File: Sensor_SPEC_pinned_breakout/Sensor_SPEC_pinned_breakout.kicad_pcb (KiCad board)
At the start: 2 copper layers, 42 x 26 mm, 5 parts, among them P1 CONN_01X04, U1 SPEC, U2 SMM-102-02-S-S, U3 SMM-102-02-S-S, U4 SMM-102-02-S-S

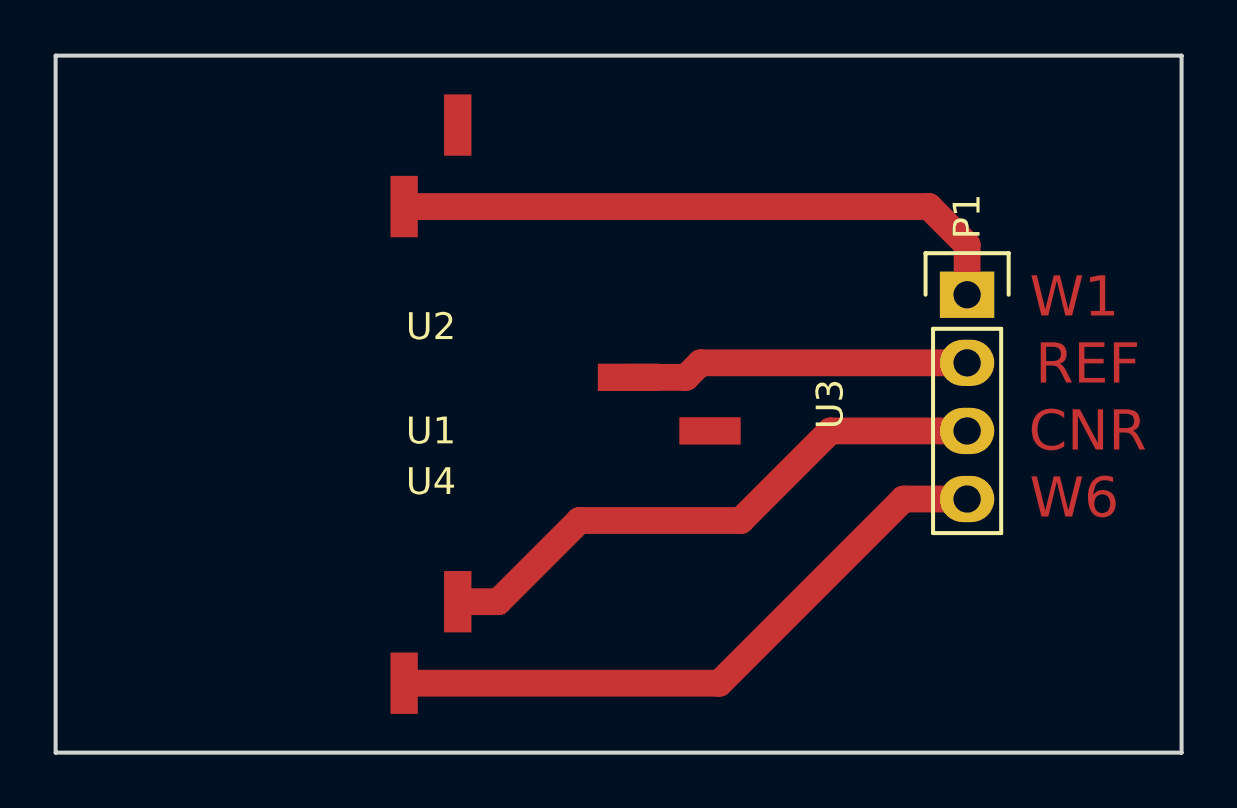
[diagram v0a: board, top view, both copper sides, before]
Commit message: changed SPEC pinned breakout
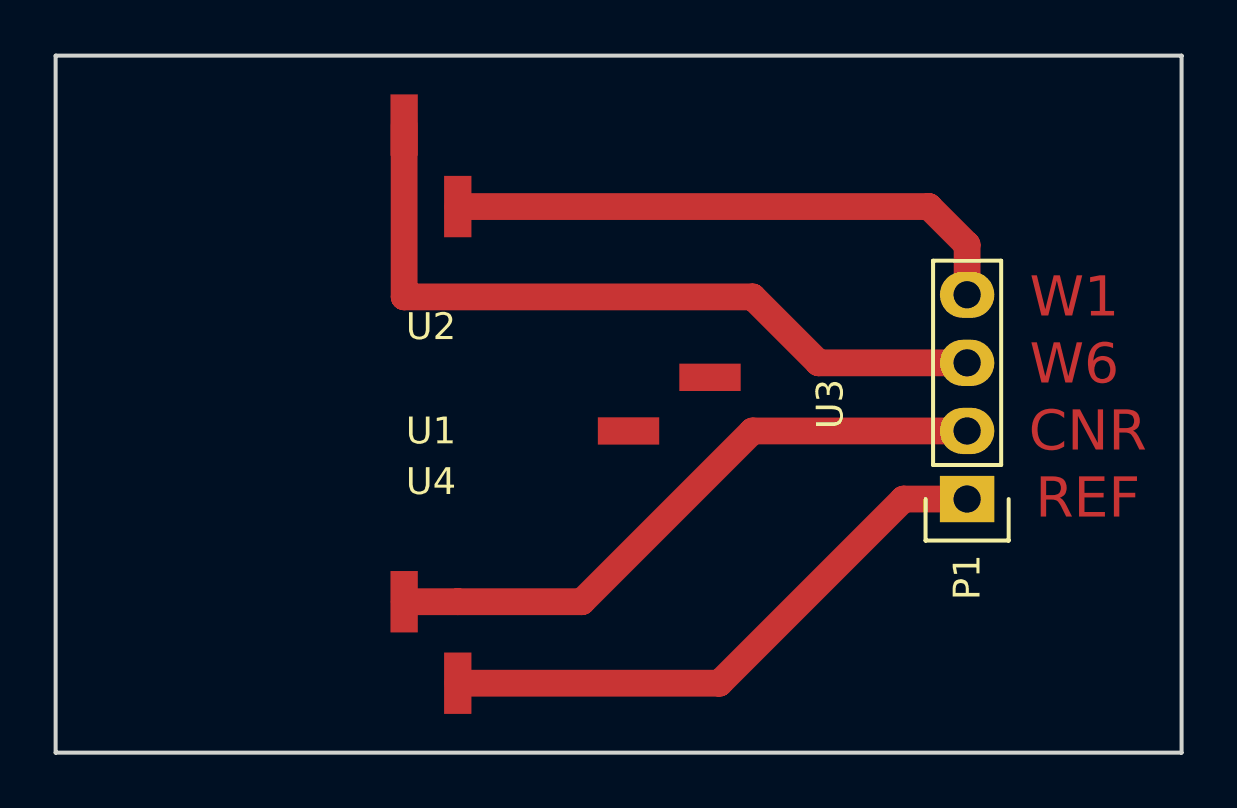
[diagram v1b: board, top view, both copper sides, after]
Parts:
- moved P1 7.62 mm to (168.0, 110.5), turned to 90 degrees
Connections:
- P1 pad 1: WORKING_1 -> REFERENCE
- P1 pad 2: REFERENCE -> COUNTER
- P1 pad 3: COUNTER -> WORKING_6
- P1 pad 4: WORKING_6 -> WORKING_1
- U2 pad 2: Net-(U2-Pad2) -> WORKING_6
- U3 pad 2: REFERENCE -> Net-(U3-Pad2)
- U4 pad 2: WORKING_6 -> REFERENCE
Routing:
- net REFERENCE: track 12.9 -> 21.8 mm
- net WORKING_6: track 23.8 -> 28.4 mm
- net WORKING_1: track 23.5 -> 21.5 mm
- net COUNTER: track 21.6 -> 23.6 mm
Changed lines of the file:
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@@
     (links 4)
     (no_connects 0)
-    (area 0 0 0 0)
+    (area 133.924999 93.924999 176.075001 120.075001)
     (thickness 1.6)
     (drawings 8)
@@
     (visible_elements FFFFFF7F)
     (pcbplotparams
-      (layerselection 0x00030_80000001)
+      (layerselection 0x01000_00000001)
       (usegerberextensions false)
       (excludeedgelayer true)
@@
       (outputformat 1)
       (mirror false)
-      (drillshape 1)
+      (drillshape 0)
       (scaleselection 1)
-      (outputdirectory ""))
+      (outputdirectory gerbers/))
   )
   (net 0 "")
@@
   (net 3 COUNTER)
   (net 4 WORKING_6)
-  (net 5 "Net-(U2-Pad2)")
-  (net 6 "Net-(U3-Pad1)")
+  (net 5 "Net-(U3-Pad1)")
+  (net 6 "Net-(U3-Pad2)")
   (net_class Default "This is the default net class."
     (clearance 0.2)
@@
     (uvia_drill 0.1)
     (add_net COUNTER)
-    (add_net "Net-(U2-Pad2)")
     (add_net "Net-(U3-Pad1)")
+    (add_net "Net-(U3-Pad2)")
     (add_net REFERENCE)
     (add_net WORKING_1)
@@
   )
   (module Socket_Strips:Socket_Strip_Straight_1x04 (layer F.Cu)
-    (at 168 102.92 270)
+    (at 168 110.54 90)
     (descr "Through hole socket strip")
     (tags "socket strip")
-    (fp_text reference P1 (at -2.92 0 270) (layer F.SilkS)
-      (effects (font (size 1 1) (thickness 0.15)))
-    )
-    (fp_text value CONN_01X04 (at 4.08 3 270) (layer F.Fab)
+    (fp_text reference P1 (at -2.92 0 90) (layer F.SilkS)
+      (effects (font (size 1 1) (thickness 0.15)))
+    )
+    (fp_text value CONN_01X04 (at 4.08 -3 90) (layer F.Fab)
       (effects (font (size 1 1) (thickness 0.15)))
     )
@@
     (fp_line (start 0 -1.55) (end -1.55 -1.55) (layer F.SilkS) (width 0.15))
     (fp_line (start -1.55 -1.55) (end -1.55 1.55) (layer F.SilkS) (width 0.15))
-    (pad 1 thru_hole rect (at 0 0 270) (size 1.7272 2.032) (drill 1.016) (layers *.Cu *.Mask F.SilkS)
+    (pad 1 thru_hole rect (at 0 0 90) (size 1.7272 2.032) (drill 1.016) (layers *.Cu *.Mask F.SilkS)
+      (net 2 REFERENCE))
+    (pad 2 thru_hole oval (at 2.54 0 90) (size 1.7272 2.032) (drill 1.016) (layers *.Cu *.Mask F.SilkS)
+      (net 3 COUNTER))
+    (pad 3 thru_hole oval (at 5.08 0 90) (size 1.7272 2.032) (drill 1.016) (layers *.Cu *.Mask F.SilkS)
+      (net 4 WORKING_6))
+    (pad 4 thru_hole oval (at 7.62 0 90) (size 1.7272 2.032) (drill 1.016) (layers *.Cu *.Mask F.SilkS)
       (net 1 WORKING_1))
-    (pad 2 thru_hole oval (at 2.54 0 270) (size 1.7272 2.032) (drill 1.016) (layers *.Cu *.Mask F.SilkS)
-      (net 2 REFERENCE))
-    (pad 3 thru_hole oval (at 5.08 0 270) (size 1.7272 2.032) (drill 1.016) (layers *.Cu *.Mask F.SilkS)
-      (net 3 COUNTER))
-    (pad 4 thru_hole oval (at 7.62 0 270) (size 1.7272 2.032) (drill 1.016) (layers *.Cu *.Mask F.SilkS)
-      (net 4 WORKING_6))
     (model Socket_Strips.3dshapes/Socket_Strip_Straight_1x04.wrl
       (at (xyz 0.15 0 0))
@@
       (effects (font (size 1 1) (thickness 0.15)))
     )
-    (pad 1 smd rect (at -1 1.52) (size 1.02 2.29) (layers F.Cu F.Paste F.Mask)
+    (pad 1 smd rect (at 1 1.52) (size 1.02 2.29) (layers F.Cu F.Paste F.Mask)
       (net 1 WORKING_1))
-    (pad 2 smd rect (at 1 -1.52) (size 1.02 2.29) (layers F.Cu F.Paste F.Mask)
-      (net 5 "Net-(U2-Pad2)"))
+    (pad 2 smd rect (at -1 -1.52) (size 1.02 2.29) (layers F.Cu F.Paste F.Mask)
+      (net 4 WORKING_6))
+  )
+  (module scintilla:SMM-102-02-S-S (layer F.Cu)
+    (at 148 115.89 180)
+    (fp_text reference U4 (at 0 6 180) (layer F.SilkS)
+      (effects (font (size 1 1) (thickness 0.15)))
+    )
+    (fp_text value SMM-102-02-S-S (at 0 -6 180) (layer F.Fab)
+      (effects (font (size 1 1) (thickness 0.15)))
+    )
+    (pad 1 smd rect (at 1 1.52 180) (size 1.02 2.29) (layers F.Cu F.Paste F.Mask)
+      (net 3 COUNTER))
+    (pad 2 smd rect (at -1 -1.52 180) (size 1.02 2.29) (layers F.Cu F.Paste F.Mask)
+      (net 2 REFERENCE))
   )
   (module scintilla:SMM-102-02-S-S (layer F.Cu)
@@
       (effects (font (size 1 1) (thickness 0.15)))
     )
-    (pad 1 smd rect (at -1 1.52 90) (size 1.02 2.29) (layers F.Cu F.Paste F.Mask)
-      (net 6 "Net-(U3-Pad1)"))
-    (pad 2 smd rect (at 1 -1.52 90) (size 1.02 2.29) (layers F.Cu F.Paste F.Mask)
-      (net 2 REFERENCE))
-  )
-  (module scintilla:SMM-102-02-S-S (layer F.Cu)
-    (at 148 115.89 180)
-    (fp_text reference U4 (at 0 6 180) (layer F.SilkS)
-      (effects (font (size 1 1) (thickness 0.15)))
-    )
-    (fp_text value SMM-102-02-S-S (at 0 -6 180) (layer F.Fab)
-      (effects (font (size 1 1) (thickness 0.15)))
-    )
-    (pad 1 smd rect (at -1 1.52 180) (size 1.02 2.29) (layers F.Cu F.Paste F.Mask)
-      (net 3 COUNTER))
-    (pad 2 smd rect (at 1 -1.52 180) (size 1.02 2.29) (layers F.Cu F.Paste F.Mask)
-      (net 4 WORKING_6))
+    (pad 1 smd rect (at 1 1.52 90) (size 1.02 2.29) (layers F.Cu F.Paste F.Mask)
+      (net 5 "Net-(U3-Pad1)"))
+    (pad 2 smd rect (at -1 -1.52 90) (size 1.02 2.29) (layers F.Cu F.Paste F.Mask)
+      (net 6 "Net-(U3-Pad2)"))
+  )
+  (gr_text REF (at 172.5 110.5) (layer F.Cu)
+    (effects (font (size 1.5 1.5) (thickness 0.3)))
   )
   (gr_line (start 134 120) (end 134 94) (layer Edge.Cuts) (width 0.15))
@@
   (gr_line (start 176 94) (end 176 120) (layer Edge.Cuts) (width 0.15))
   (gr_line (start 134 94) (end 176 94) (layer Edge.Cuts) (width 0.15))
-  (gr_text W6 (at 172 110.5) (layer F.Cu)
+  (gr_text W6 (at 172 105.5) (layer F.Cu)
     (effects (font (size 1.5 1.5) (thickness 0.3)))
   )
@@
     (effects (font (size 1.5 1.5) (thickness 0.3)))
   )
-  (gr_text REF (at 172.5 105.5) (layer F.Cu)
-    (effects (font (size 1.5 1.5) (thickness 0.3)))
-  )
   (gr_text W1 (at 172 103) (layer F.Cu)
     (effects (font (size 1.5 1.5) (thickness 0.3)))
   )
-  (segment (start 147 99.63) (end 166.5736 99.63) (width 1) (layer F.Cu) (net 1))
+  (segment (start 166.5736 99.63) (end 149 99.63) (width 1) (layer F.Cu) (net 1))
   (segment (start 166.5736 99.63) (end 168 101.0564) (width 1) (layer F.Cu) (net 1))
   (segment (start 168 101.0564) (end 168 102.92) (width 1) (layer F.Cu) (net 1))
-  (segment (start 157.515 106) (end 158.055 105.46) (width 1) (layer F.Cu) (net 2))
-  (segment (start 158.055 105.46) (end 168 105.46) (width 1) (layer F.Cu) (net 2))
-  (segment (start 155.37 106) (end 157.515 106) (width 1) (layer F.Cu) (net 2))
-  (segment (start 159.56 111.34) (end 162.9 108) (width 1) (layer F.Cu) (net 3))
-  (segment (start 162.9 108) (end 168 108) (width 1) (layer F.Cu) (net 3))
-  (segment (start 153.54 111.34) (end 159.56 111.34) (width 1) (layer F.Cu) (net 3))
-  (segment (start 149 114.37) (end 150.51 114.37) (width 1) (layer F.Cu) (net 3))
-  (segment (start 150.51 114.37) (end 153.54 111.34) (width 1) (layer F.Cu) (net 3))
-  (segment (start 158.76 117.41) (end 165.63 110.54) (width 1) (layer F.Cu) (net 4))
-  (segment (start 165.63 110.54) (end 168 110.54) (width 1) (layer F.Cu) (net 4))
-  (segment (start 147 117.41) (end 158.76 117.41) (width 1) (layer F.Cu) (net 4))
+  (segment (start 165.63 110.54) (end 168 110.54) (width 1) (layer F.Cu) (net 2))
+  (segment (start 158.76 117.41) (end 165.63 110.54) (width 1) (layer F.Cu) (net 2))
+  (segment (start 158.76 117.41) (end 149 117.41) (width 1) (layer F.Cu) (net 2))
+  (segment (start 149 114.37) (end 147 114.37) (width 1) (layer F.Cu) (net 3))
+  (segment (start 168 108) (end 160 108) (width 1) (layer F.Cu) (net 3))
+  (segment (start 160 108) (end 153.63 114.37) (width 1) (layer F.Cu) (net 3))
+  (segment (start 153.63 114.37) (end 149 114.37) (width 1) (layer F.Cu) (net 3))
+  (segment (start 168 105.46) (end 162.46 105.46) (width 1) (layer F.Cu) (net 4))
+  (segment (start 147 103) (end 147 96.59) (width 1) (layer F.Cu) (net 4))
+  (segment (start 162.46 105.46) (end 160 103) (width 1) (layer F.Cu) (net 4))
+  (segment (start 160 103) (end 147 103) (width 1) (layer F.Cu) (net 4))
 )
